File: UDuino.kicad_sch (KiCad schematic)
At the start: 2 parts, among them U4 STM32L452VCTx

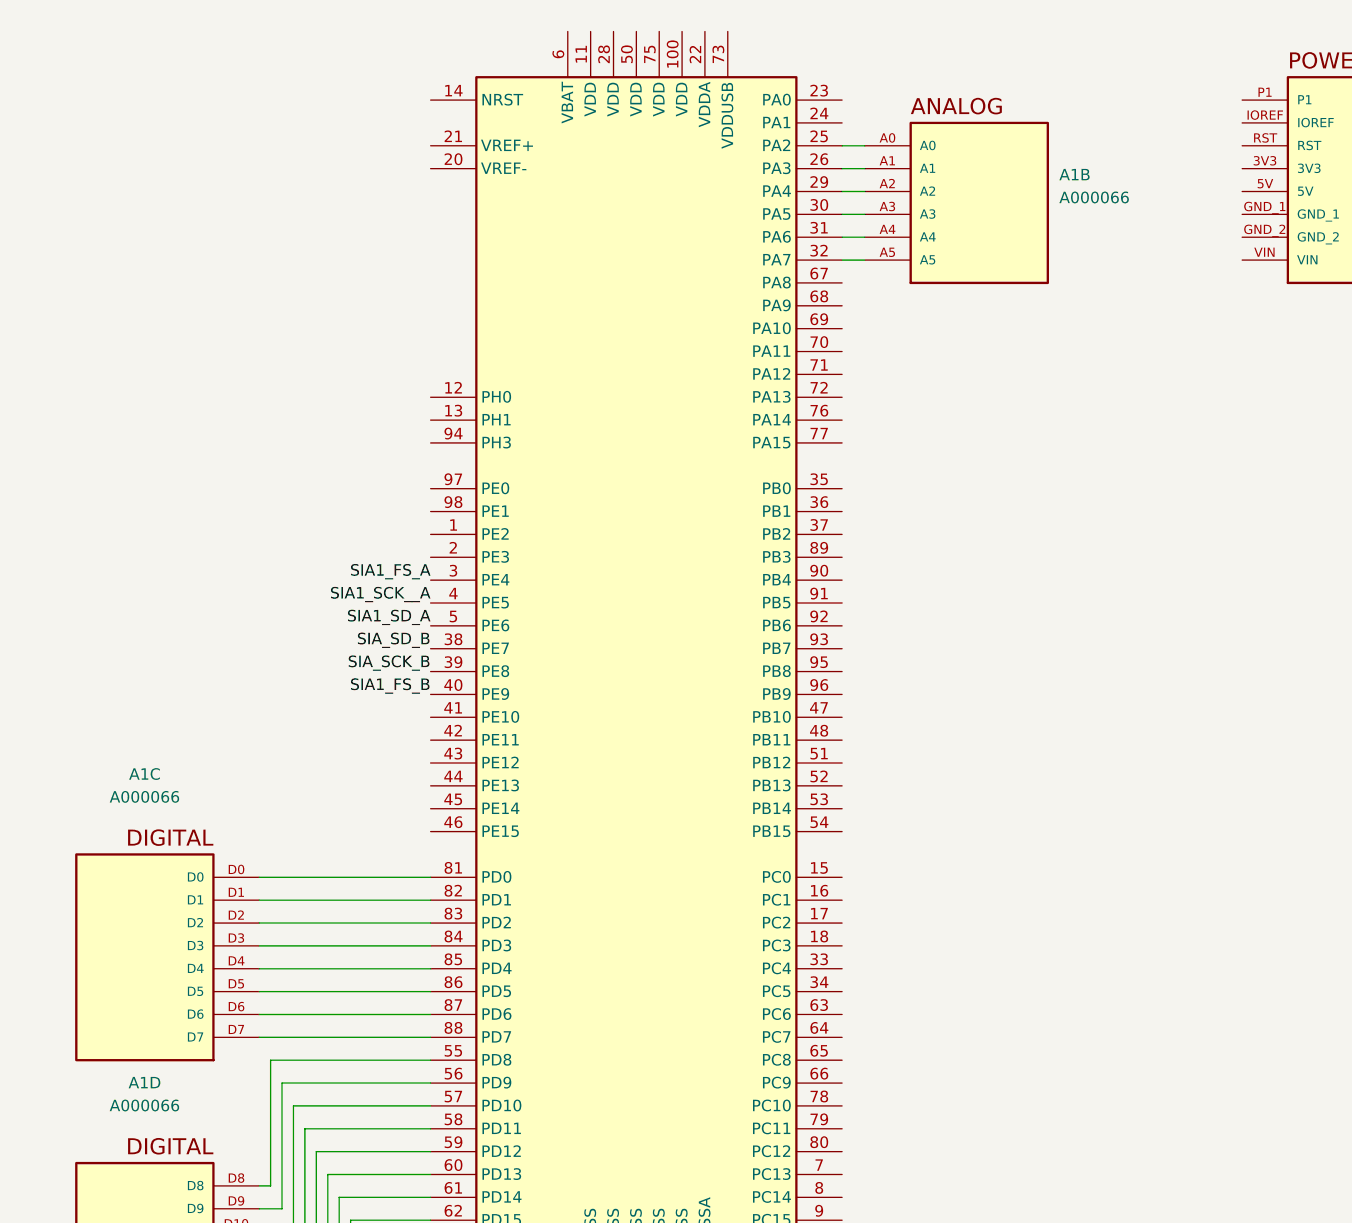
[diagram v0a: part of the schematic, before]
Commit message: Rough placement of Speakers on board
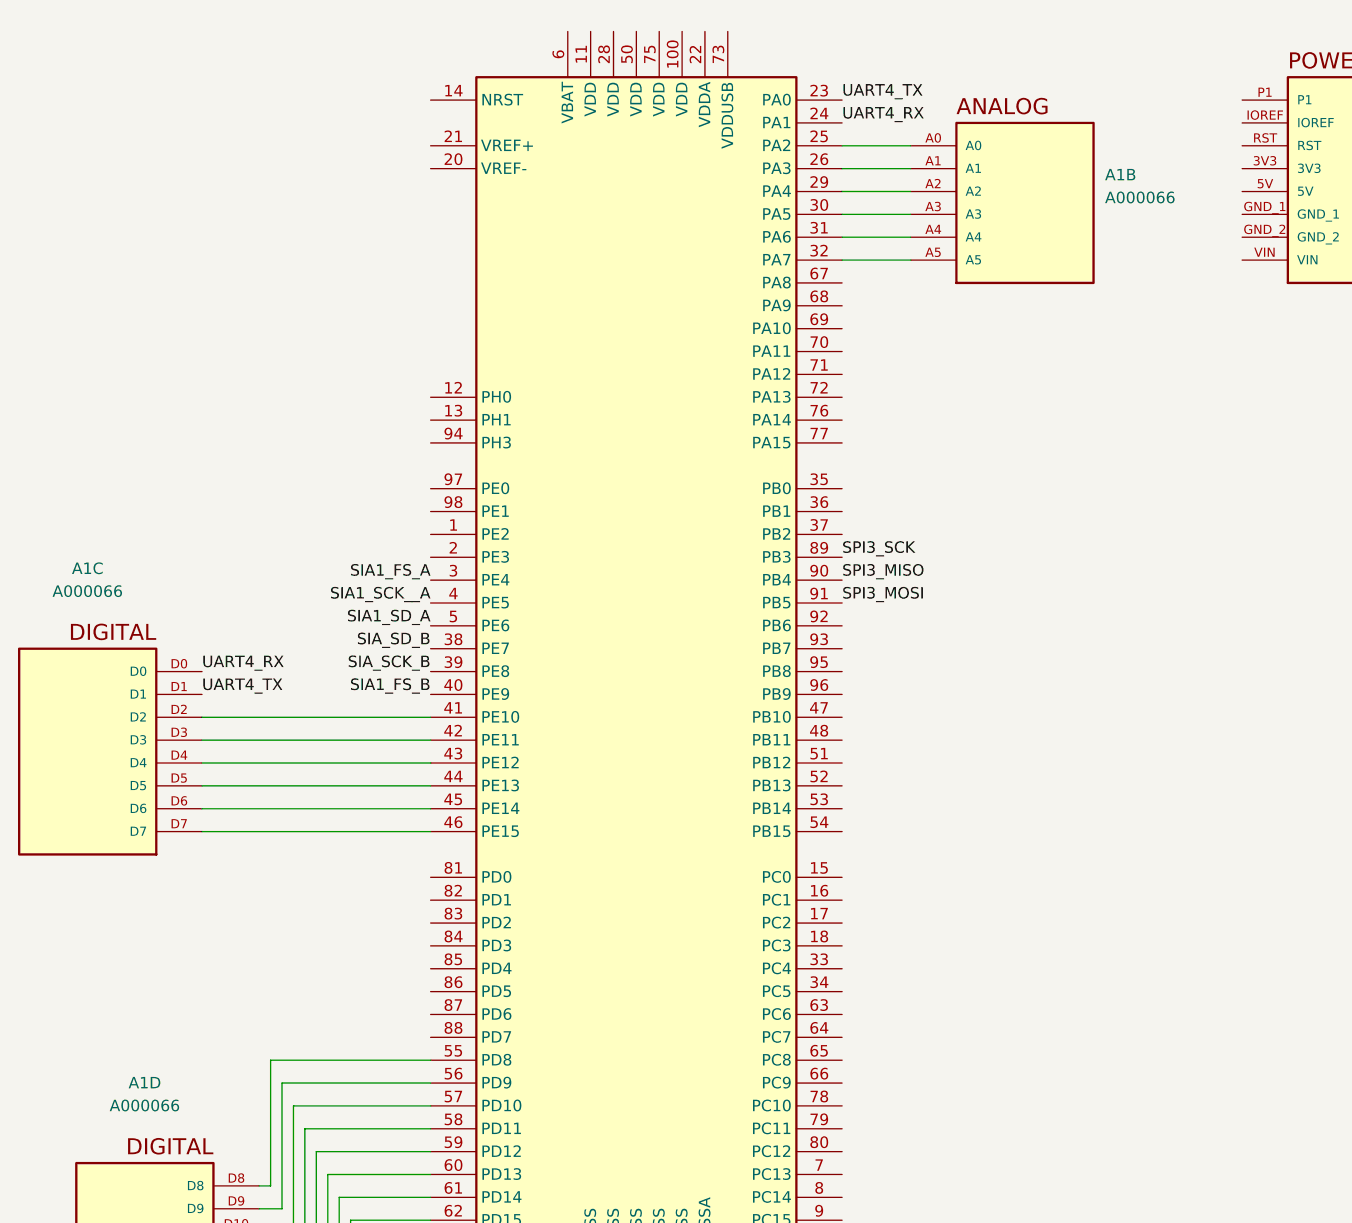
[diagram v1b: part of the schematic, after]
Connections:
- net at U4.81 (PD0): no longer A1.D0
- net at U4.82 (PD1): no longer A1.D1
- net at A1.D2: now also U4.41 (PE10); no longer U4.83 (PD2)
- net at A1.D3: now also U4.42 (PE11); no longer U4.84 (PD3)
- net at A1.D4: now also U4.43 (PE12); no longer U4.85 (PD4)
- net at A1.D5: now also U4.44 (PE13); no longer U4.86 (PD5)
- net at A1.D6: now also U4.45 (PE14); no longer U4.87 (PD6)
- net at A1.D7: now also U4.46 (PE15); no longer U4.88 (PD7)
- net UART4_TX: now reaches U4.23 (PA0)
- net UART4_TX: now also A1.D1
- net UART4_RX: now reaches U4.24 (PA1)
- net UART4_RX: now also A1.D0
- net SPI3_SCK: now reaches U4.89 (PB3)
- net SPI3_MISO: now reaches U4.90 (PB4)
- net SPI3_MOSI: now reaches U4.91 (PB5)
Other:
- moved on the sheet: A1B, A1C

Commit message: Rough placement of the Motor controller
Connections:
- net Motor/AIN1: now also U4.15 (PC0)
- net Motor/AIN2: now also U4.16 (PC1)
- net Motor/BIN1: now also U4.18 (PC3)
- net Motor/BIN2: now also U4.17 (PC2)
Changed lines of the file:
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@@
+    (stroke (width 0) (type default) (color 0 0 0 0))
+  )
+  (wire (pts (xy 118.11 123.19) (xy 130.81 123.19))
     (stroke (width 0) (type default) (color 0 0 0 0))
   )
@@
     (stroke (width 0) (type default) (color 0 0 0 0))
   )
+  (wire (pts (xy 118.11 120.65) (xy 130.81 120.65))
+    (stroke (width 0) (type default) (color 0 0 0 0))
+  )
+  (wire (pts (xy 118.11 125.73) (xy 130.81 125.73))
+    (stroke (width 0) (type default) (color 0 0 0 0))
+  )
   (wire (pts (xy 60.96 175.26) (xy 60.96 153.67))
     (stroke (width 0) (type default) (color 0 0 0 0))
@@
   )
   (wire (pts (xy 125.73 44.45) (xy 118.11 44.45))
+    (stroke (width 0) (type default) (color 0 0 0 0))
+  )
+  (wire (pts (xy 118.11 128.27) (xy 130.81 128.27))
     (stroke (width 0) (type default) (color 0 0 0 0))
   )
@@
     )
   )
-  (sheet (at 245.11 132.08) (size 13.97 17.78) (fields_autoplaced)
+  (sheet (at 130.81 115.57) (size 13.97 17.78) (fields_autoplaced)
     (stroke (width 0.1524) (type solid) (color 0 0 0 0))
     (fill (color 0 0 0 0.0000))
-    (property "Sheet name" "Motor" (id 0) (at 245.11 131.3684 0)
+    (property "Sheet name" "Motor" (id 0) (at 130.81 114.8584 0)
       (effects (font (size 1.27 1.27)) (justify left bottom))
     )
-    (property "Sheet file" "Motor/Motor.kicad_sch" (id 1) (at 245.11 150.4446 0)
+    (property "Sheet file" "Motor/Motor.kicad_sch" (id 1) (at 130.81 133.9346 0)
       (effects (font (size 1.27 1.27)) (justify left top))
     )
-    (pin "nSLEEP" input (at 245.11 134.62 180)
-      (effects (font (size 1.27 1.27)) (justify left))
-    )
-    (pin "nFAULT" output (at 245.11 147.32 180)
-      (effects (font (size 1.27 1.27)) (justify left))
-    )
-    (pin "AIN1" input (at 245.11 137.16 180)
-      (effects (font (size 1.27 1.27)) (justify left))
-    )
-    (pin "AIN2" input (at 245.11 139.7 180)
-      (effects (font (size 1.27 1.27)) (justify left))
-    )
-    (pin "BIN1" input (at 245.11 142.24 180)
-      (effects (font (size 1.27 1.27)) (justify left))
-    )
-    (pin "BIN2" input (at 245.11 144.78 180)
-      (effects (font (size 1.27 1.27)) (justify left))
-    )
+    (pin "nSLEEP" input (at 130.81 118.11 180)
+      (effects (font (size 1.27 1.27)) (justify left))
+    )
+    (pin "nFAULT" output (at 130.81 130.81 180)
+      (effects (font (size 1.27 1.27)) (justify left))
+    )
+    (pin "AIN1" input (at 130.81 120.65 180)
+      (effects (font (size 1.27 1.27)) (justify left))
+    )
+    (pin "AIN2" input (at 130.81 123.19 180)
+      (effects (font (size 1.27 1.27)) (justify left))
+    )
+    (pin "BIN2" input (at 130.81 125.73 180)
+      (effects (font (size 1.27 1.27)) (justify left))
+    )
+    (pin "BIN1" input (at 130.81 128.27 180)
+      (effects (font (size 1.27 1.27)) (justify left))
+    )

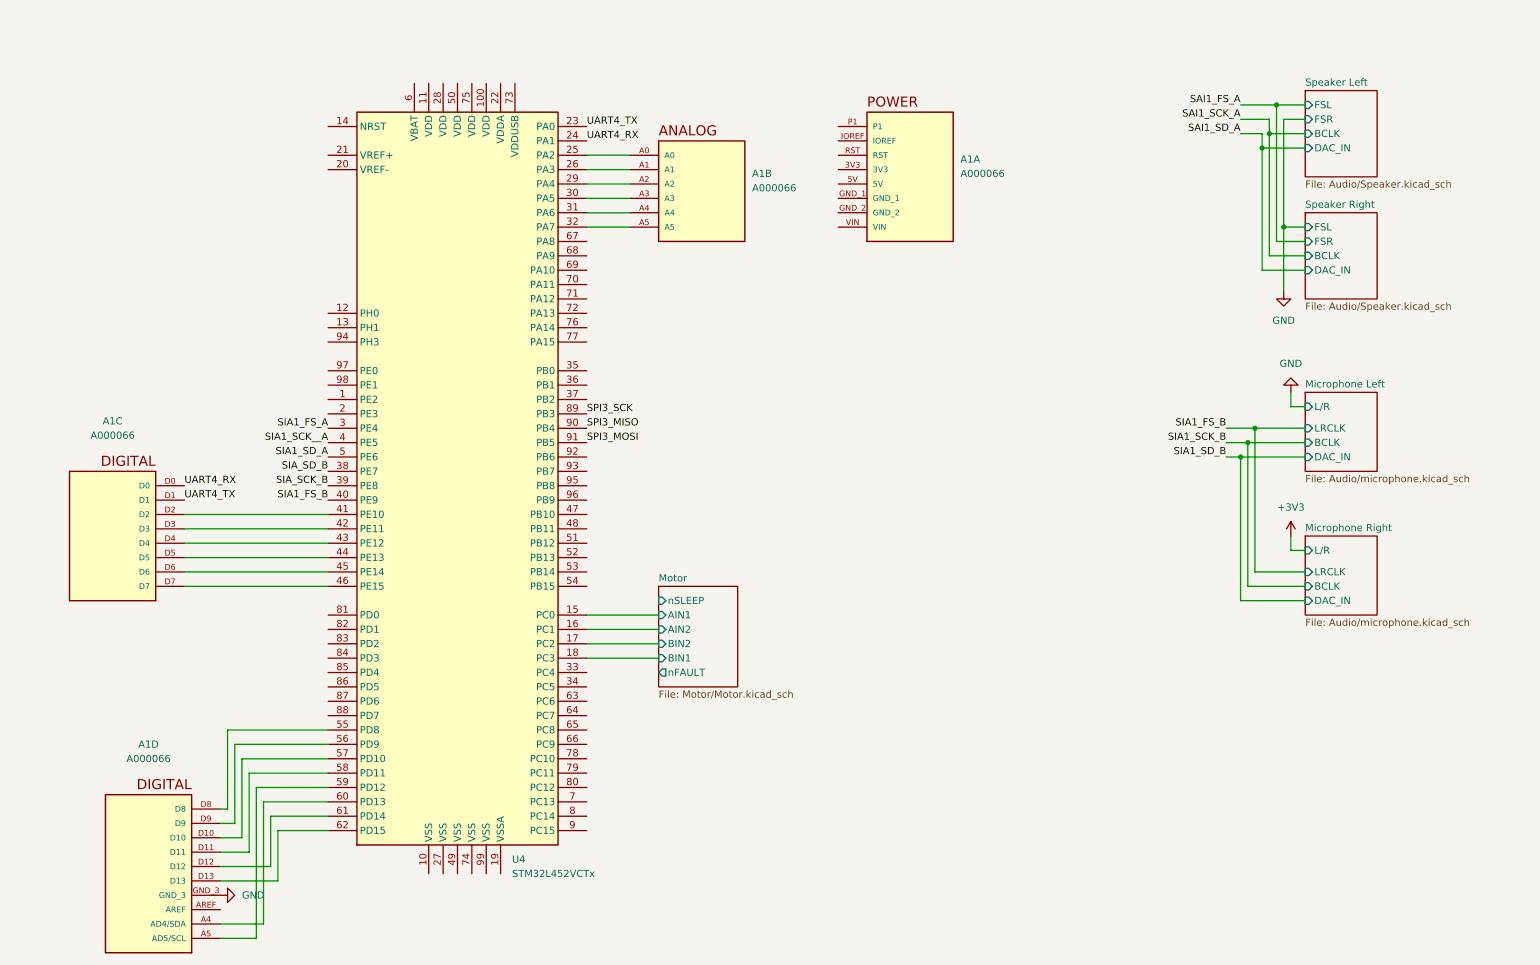
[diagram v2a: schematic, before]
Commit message: Added Switches, Buttons, LEDs, 7Seg, LCD
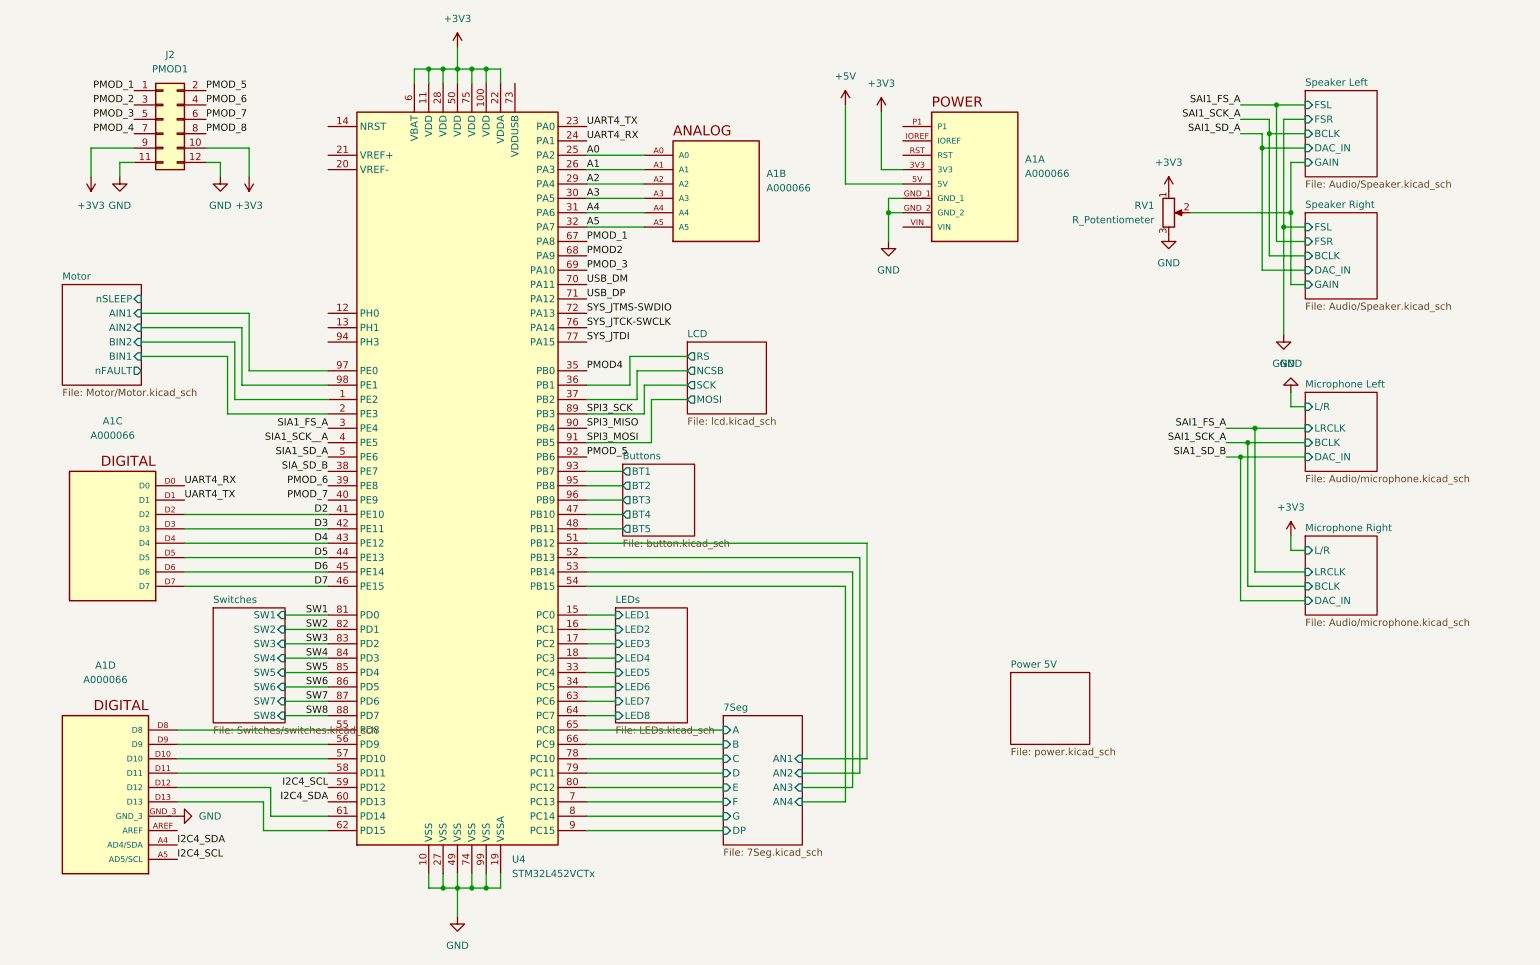
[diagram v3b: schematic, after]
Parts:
- added J2: PMOD1, Connector_PinSocket_2.54mm:PinSocket_2x06_P2.54mm_Horizontal, symbol Connector_Generic:Conn_02x06_Odd_Even
- added RV1: R_Potentiometer, Custom:TRIM_3352T-1-104LF, symbol Device:R_Potentiometer
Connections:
- net +3V3: now also A1.3V3, U4.100 (VDD), U4.11 (VDD), U4.22 (VDDA), U4.28 (VDD), U4.50 (VDD), U4.6 (VBAT), U4.75 (VDD), J2.10 (Pin_10), J2.9 (Pin_9), RV1.1
- net GND: now also A1.GND_1, A1.GND_2, U4.10 (VSS), U4.19 (VSSA), U4.27 (VSS), U4.49 (VSS), U4.74 (VSS), U4.99 (VSS), J2.11 (Pin_11), J2.12 (Pin_12), RV1.3
- net Motor/AIN1: now also U4.97 (PE0); no longer U4.15 (PC0)
- net Motor/AIN2: now also U4.98 (PE1); no longer U4.16 (PC1)
- net Motor/BIN1: now also U4.2 (PE3); no longer U4.18 (PC3)
- net Motor/BIN2: now also U4.1 (PE2); no longer U4.17 (PC2)
- net D2: now reaches A1.D2, U4.41 (PE10)
- net D3: now reaches A1.D3, U4.42 (PE11)
- net D4: now reaches A1.D4, U4.43 (PE12)
- net D5: now reaches A1.D5, U4.44 (PE13)
- net D6: now reaches A1.D6, U4.45 (PE14)
- net D7: now reaches A1.D7, U4.46 (PE15)
- net A0: now reaches A1.A0, U4.25 (PA2)
- net A1: now reaches A1.A1, U4.26 (PA3)
- net A2: now reaches A1.A2, U4.29 (PA4)
- net A3: now reaches A1.A3, U4.30 (PA5)
- net A4: now reaches A1.A4, U4.31 (PA6)
- net A5: now reaches A1.A5, U4.32 (PA7)
- net I2C4_SDA: now reaches A1.A4 (AD4/SDA), U4.60 (PD13)
- net I2C4_SCL: now reaches A1.A5 (AD5/SCL), U4.59 (PD12)
- net +5V: now reaches A1.5V
- net LEDs/LED5: now reaches U4.33 (PC4)
- net LEDs/LED6: now reaches U4.34 (PC5)
- net PMOD4: now reaches U4.35 (PB0)
- net LCD/RS: now reaches U4.36 (PB1)
- net LCD/NCSB: now reaches U4.37 (PB2)
- net Buttons/BT4: now reaches U4.47 (PB10)
- net Buttons/BT5: now reaches U4.48 (PB11)
- net 7Seg/AN1: now reaches U4.51 (PB12)
- net 7Seg/AN2: now reaches U4.52 (PB13)
- net 7Seg/AN3: now reaches U4.53 (PB14)
- net 7Seg/AN4: now reaches U4.54 (PB15)
- net LEDs/LED7: now reaches U4.63 (PC6)
- net LEDs/LED8: now reaches U4.64 (PC7)
- net 7Seg/A: now reaches U4.65 (PC8)
- net 7Seg/B: now reaches U4.66 (PC9)
- net PMOD_1: now reaches U4.67 (PA8)
- net PMOD_1: now also J2.1 (Pin_1)
- net PMOD2: now reaches U4.68 (PA9)
- net PMOD_3: now reaches U4.69 (PA10)
- net PMOD_3: now also J2.5 (Pin_5)
- net 7Seg/F: now reaches U4.7 (PC13)
- net USB_DM: now reaches U4.70 (PA11)
- net USB_DP: now reaches U4.71 (PA12)
- net SYS_JTMS-SWDIO: now reaches U4.72 (PA13)
- net SYS_JTCK-SWCLK: now reaches U4.76 (PA14)
- net SYS_JTDI: now reaches U4.77 (PA15)
- net 7Seg/C: now reaches U4.78 (PC10)
- net 7Seg/D: now reaches U4.79 (PC11)
- net 7Seg/G: now reaches U4.8 (PC14)
- net 7Seg/E: now reaches U4.80 (PC12)
- net SW1: now reaches U4.81 (PD0)
- net SW2: now reaches U4.82 (PD1)
- net SW3: now reaches U4.83 (PD2)
- net SW4: now reaches U4.84 (PD3)
- net SW5: now reaches U4.85 (PD4)
- net SW6: now reaches U4.86 (PD5)
- net SW7: now reaches U4.87 (PD6)
- net SW8: now reaches U4.88 (PD7)
- net 7Seg/DP: now reaches U4.9 (PC15)
- net PMOD_5: now reaches U4.92 (PB6)
- net PMOD_5: now also J2.2 (Pin_2)
- net Buttons/BT1: now reaches U4.93 (PB7)
- net Buttons/BT2: now reaches U4.95 (PB8)
- net Buttons/BT3: now reaches U4.96 (PB9)
- net SIA1_FS_B renamed PMOD_7
- net PMOD_7: now also J2.6 (Pin_6)
- net SIA_SCK_B renamed PMOD_6
- net PMOD_6: now also J2.4 (Pin_4)
- new net LEDs/LED1: U4.15 (PC0)
- new net LEDs/LED2: U4.16 (PC1)
- new net LEDs/LED3: U4.17 (PC2)
- new net LEDs/LED4: U4.18 (PC3)
- new net PMOD_2: J2.3 (Pin_3)
- new net PMOD_4: J2.7 (Pin_7)
- new net PMOD_8: J2.8 (Pin_8)
- new net Speaker Left/GAIN: RV1.2
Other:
- added sheet 7Seg (7Seg.kicad_sch)
- added sheet Buttons (button.kicad_sch)
- added sheet LCD (lcd.kicad_sch)
- added sheet LEDs (LEDs.kicad_sch)
- added sheet Power 5V (power.kicad_sch)
- added sheet Switches (Switches/switches.kicad_sch)
- sheet Speaker Left ports: added GAIN; removed none
- sheet Speaker Right ports: added GAIN; removed none
- moved on the sheet: A1A, A1B, A1D

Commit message: Update board design
5v and 3v3 power blocks wired up.
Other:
- added sheet Power 3V3 (power_3v3.kicad_sch)

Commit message: Routing of some wires
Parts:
- added J3, J4: Conn_01x04_Male, Connector_PinHeader_2.54mm:PinHeader_1x04_P2.54mm_Vertical, symbol Connector:Conn_01x04_Male
- added J5, J6: Conn_01x03_Male, Connector_PinHeader_2.54mm:PinHeader_1x03_P2.54mm_Vertical, symbol Connector:Conn_01x03_Male
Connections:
- net +3V3: now also J3.1 (Pin_1), J4.1 (Pin_1), J5.1 (Pin_1), J6.1 (Pin_1)
- net A2: now also J5.2 (Pin_2)
- net A3: now also J6.2 (Pin_2)
- net D2: now also J4.2 (Pin_2)
- net D3: now also J4.3 (Pin_3)
- net D4: now also J3.2 (Pin_2)
- net D5: now also J3.3 (Pin_3)
- net GND: now also J3.4 (Pin_4), J4.4 (Pin_4), J5.3 (Pin_3), J6.3 (Pin_3)
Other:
- moved on the sheet: A1B, A1C

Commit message: 06/12/2022
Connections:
- net +3V3: now also J3.2 (Pin_2), J4.2 (Pin_2), J5.2 (Pin_2), J6.2 (Pin_2); no longer J3.1 (Pin_1), J4.1 (Pin_1), J5.1 (Pin_1), J6.1 (Pin_1)
- net A2: now also J5.3 (Pin_3); no longer J5.2 (Pin_2)
- net A3: now also J6.3 (Pin_3); no longer J6.2 (Pin_2)
- net D2: now also J4.3 (Pin_3); no longer J4.2 (Pin_2)
- net D3: now also A1.D4, J3.3 (Pin_3), J4.4 (Pin_4), U4.43 (PE12); no longer J4.3 (Pin_3)
- net D5: now also J3.4 (Pin_4); no longer J3.3 (Pin_3)
- net GND: now also J3.1 (Pin_1), J4.1 (Pin_1), J5.1 (Pin_1), J6.1 (Pin_1); no longer J3.4 (Pin_4), J4.4 (Pin_4), J5.3 (Pin_3), J6.3 (Pin_3)
- removed net D4: A1.D4, J3.2 (Pin_2), U4.43 (PE12)
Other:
- moved on the sheet: RV1
